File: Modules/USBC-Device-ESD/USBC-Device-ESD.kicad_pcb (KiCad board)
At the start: 4 copper layers, 4 parts, among them J1 USB-C, U2 USBLC6-2SC6

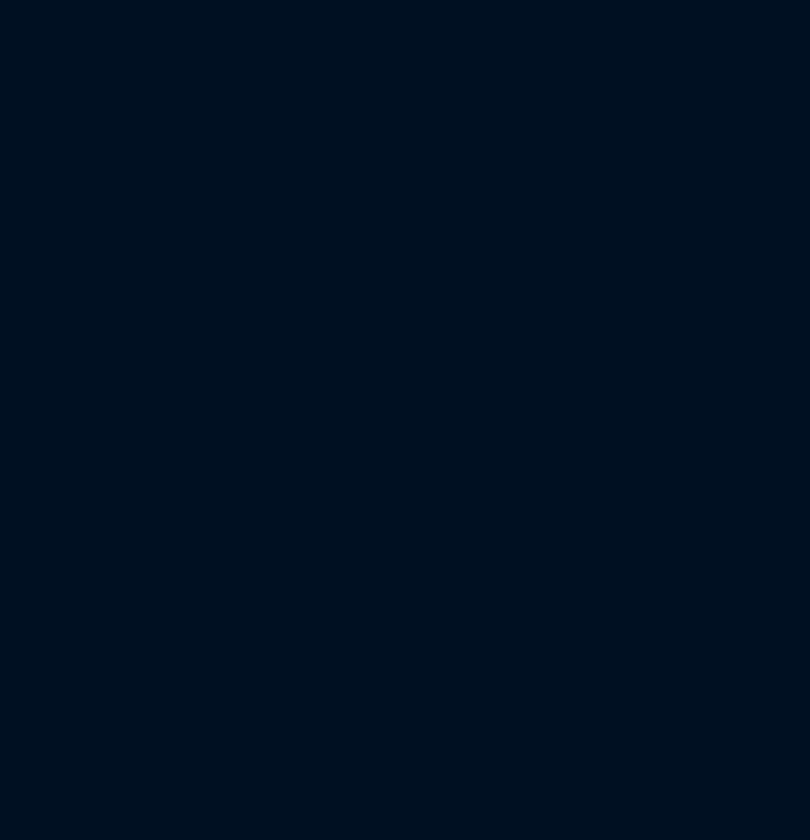
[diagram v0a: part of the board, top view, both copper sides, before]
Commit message: Add the base zones to five module boards
Whole-board zones for USBC, Buck, PowerMux, MCU and RF, written by file
before each board is opened. RF In1 carries a notch under J3 pad 1. Power
polygons become wide tracks during layout, because add_copper_pour cannot
set a zone priority.

Co-Authored-By: Claude Opus 5.5 (1M context) <noreply@anthropic.com>
Claude-Session: https://claude.ai/code/session_01ErAAfkmF4h3T5yfrw21utF
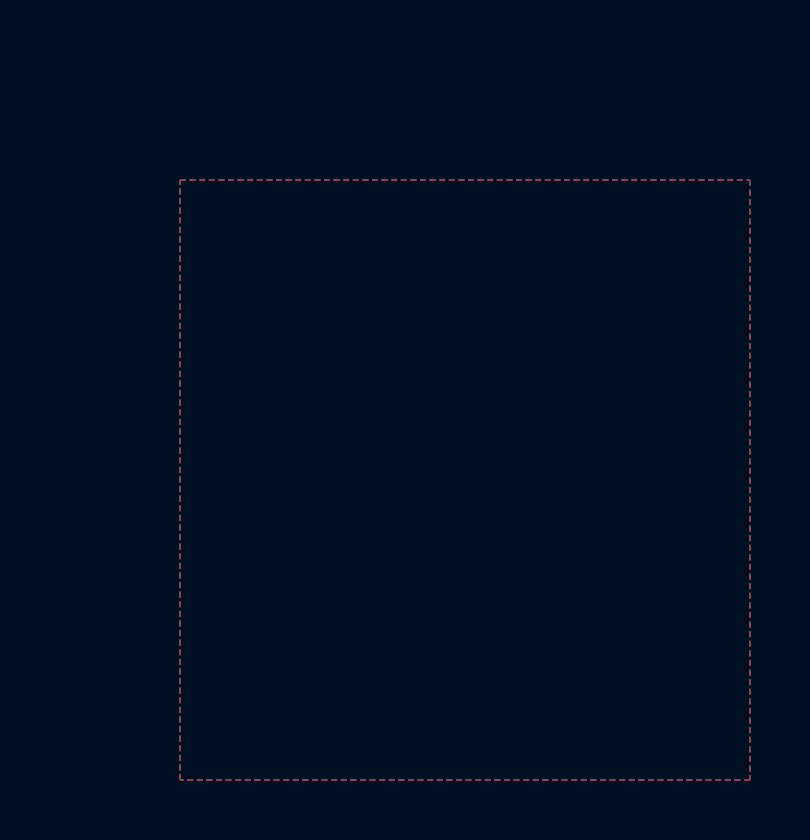
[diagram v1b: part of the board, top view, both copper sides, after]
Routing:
- added copper zone on B.Cu, net GND
- added copper zone on F.Cu, net GND
- added copper zone on In1.Cu, net GND
- added copper zone on In2.Cu, net GND
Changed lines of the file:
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@@
 	)
 	(embedded_fonts no)
-)
+  (zone (net 0) (net_name "GND") (layer "F.Cu")
+    (hatch edge 0.508)
+    (connect_pads (clearance 0.2))
+    (min_thickness 0.25)
+    (fill yes)
+    (polygon (pts
+      (xy 100.5 100.5)
+      (xy 119.5 100.5)
+      (xy 119.5 120.5)
+      (xy 100.5 120.5)
+    ))
+  )
+  (zone (net 0) (net_name "GND") (layer "In1.Cu")
+    (hatch edge 0.508)
+    (connect_pads (clearance 0.2))
+    (min_thickness 0.25)
+    (fill yes)
+    (polygon (pts
+      (xy 100.5 100.5)
+      (xy 119.5 100.5)
+      (xy 119.5 120.5)
+      (xy 100.5 120.5)
+    ))
+  )
+  (zone (net 0) (net_name "GND") (layer "In2.Cu")
+    (hatch edge 0.508)
+    (connect_pads (clearance 0.2))
+    (min_thickness 0.25)
+    (fill yes)
+    (polygon (pts
+      (xy 100.5 100.5)
+      (xy 119.5 100.5)
+      (xy 119.5 120.5)
+      (xy 100.5 120.5)
+    ))
+  )
+  (zone (net 0) (net_name "GND") (layer "B.Cu")
+    (hatch edge 0.508)
+    (connect_pads (clearance 0.2))
+    (min_thickness 0.25)
+    (fill yes)
+    (polygon (pts
+      (xy 100.5 100.5)
+      (xy 119.5 100.5)
+      (xy 119.5 120.5)
+      (xy 100.5 120.5)
+    ))
+  ))

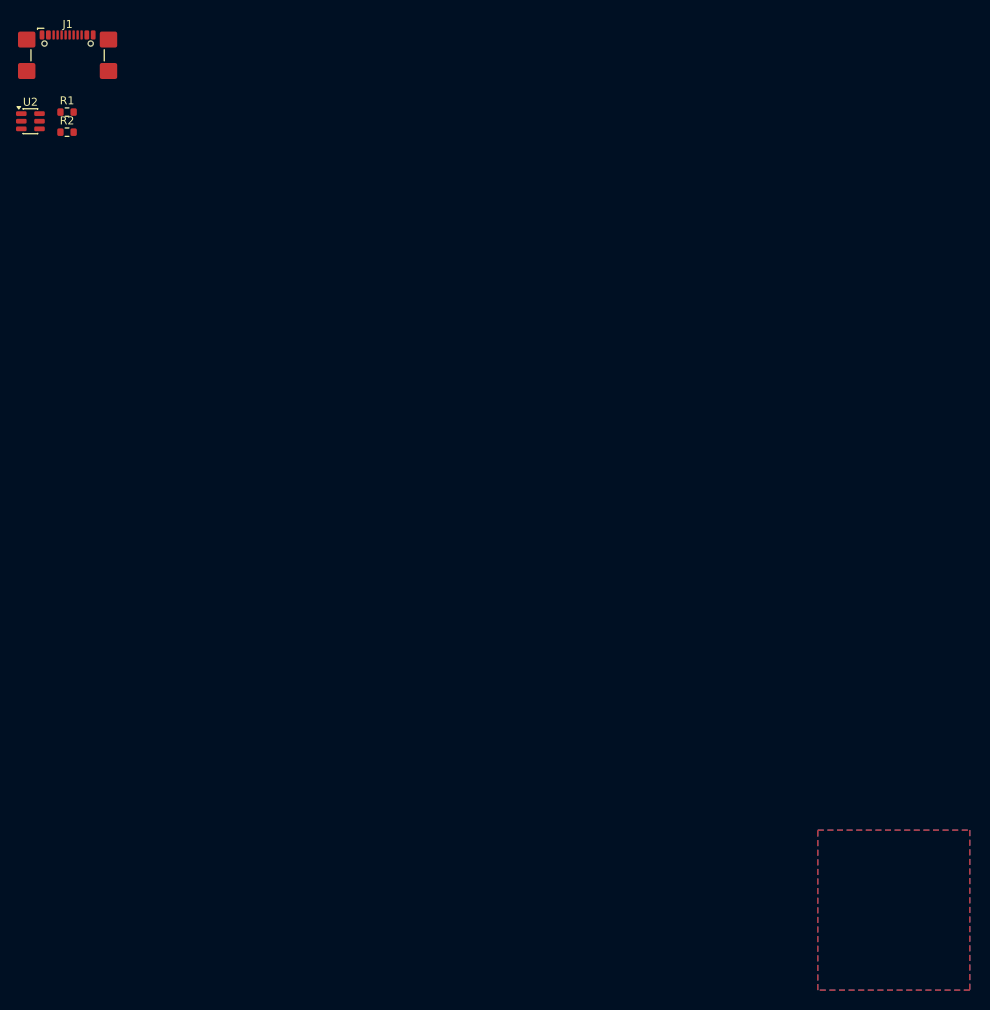
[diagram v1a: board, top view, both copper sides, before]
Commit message: Lay out the USBC-Device-ESD module
20 x 21 mm, 4 layers, GND on all four. J1 on the top edge, U2 in series in
the pair, the D+ crossing on a B.Cu jumper. VBUS at 0.508 mm with two vias
at each layer change. Breakout row at y 118.5: four GND, two VBUS, USB_DM,
USB_DP. Pair lengths 9.73 and 10.28 mm.

Rules: scope a 0.15 mm hole clearance to J1's own pads and pegs. The stock
GCT USB4110 land pattern sets them 0.194 mm apart.

DRC: 0 errors, 0 unconnected, 0 parity. The 4 track_dangling warnings are
the 4 interface stubs. Canary 8 to 252.

Co-Authored-By: Claude Opus 5.5 (1M context) <noreply@anthropic.com>
Claude-Session: https://claude.ai/code/session_01ErAAfkmF4h3T5yfrw21utF
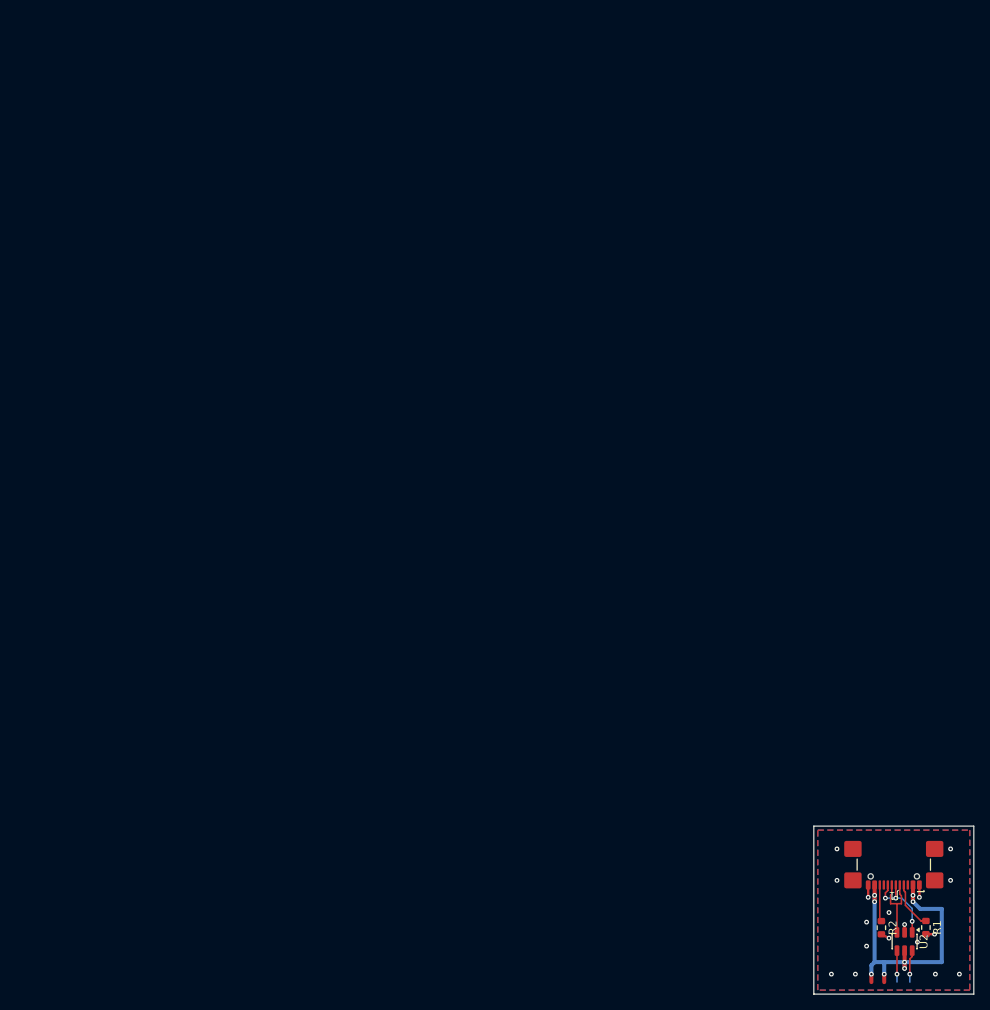
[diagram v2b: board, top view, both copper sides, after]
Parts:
- moved U2 149.8 mm to (111.3, 114.4), turned to -90 degrees
- moved R1 148.0 mm to (114.0, 112.7), turned to -90 degrees
- moved J1 143.0 mm to (110.0, 103.7), turned to 180 degrees
- moved R2 142.3 mm to (108.5, 112.7), turned to -90 degrees
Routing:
- net /VBUS: track 0.00 -> 40.6 mm, vias 0 -> 8
- net /USB_DP_CONN: track 0.00 -> 10.3 mm, vias 0 -> 3
- net /USB_DM_CONN: track 0.00 -> 9.77 mm
- net GND: track 0.00 -> 6.23 mm, vias 0 -> 17
- net /USB_CC1: track 0.00 -> 6.00 mm
- net /USB_CC2: track 0.00 -> 4.60 mm
- net /USB_DP: track 0.00 -> 4.06 mm, vias 0 -> 1
- net /USB_DM: track 0.00 -> 3.94 mm, vias 0 -> 1
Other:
- board outline added: 20 x 21 mm
- board text added: "GND"
- board text added: "USB_DM"
- board text added: "USB_DP"
- board text added: "VBUS"

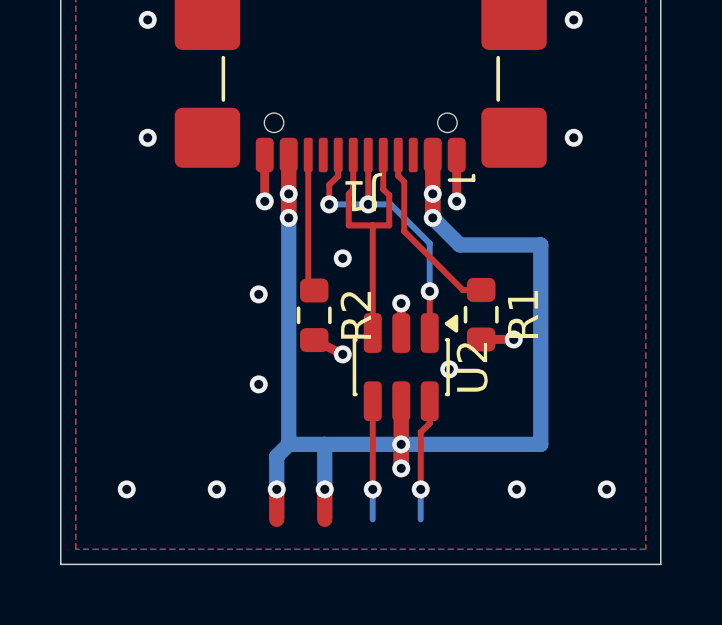
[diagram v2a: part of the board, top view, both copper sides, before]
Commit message: Restore footprints and move passive references to F.Fab
GUI batch 2a on all eight module boards. Update Footprints from Library
restores the (units) blocks that Konnect IPC writes dropped: U10, U1, SW1,
SW2 and U4 no longer report lib_footprint_mismatch. Reference designators of
C, R, L, FB, D, Y and TP parts move to F.Fab. U, J and SW stay on the silk.

Every board: DRC 0 errors, 0 unconnected, 0 parity, the canary fires, and
track_dangling equals the interface stub count.

Co-Authored-By: Claude Opus 5.5 (1M context) <noreply@anthropic.com>
Claude-Session: https://claude.ai/code/session_01ErAAfkmF4h3T5yfrw21utF
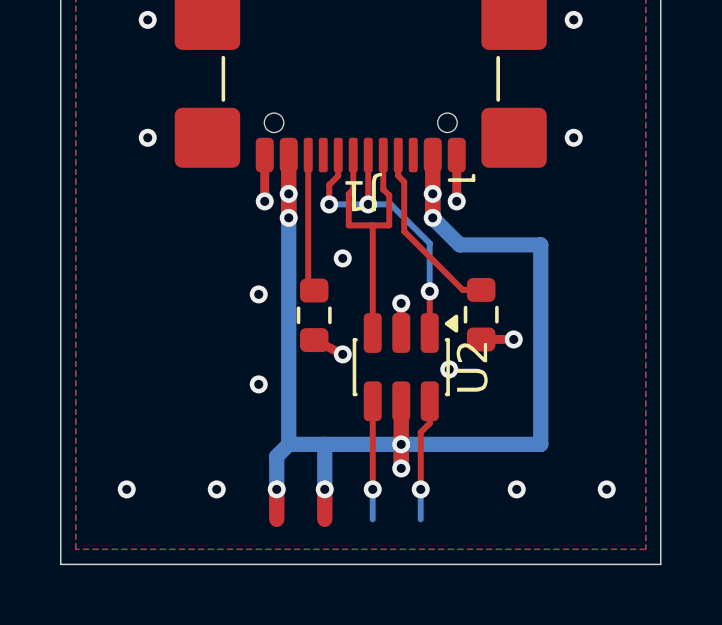
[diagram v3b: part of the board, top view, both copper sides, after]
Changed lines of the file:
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@@
 			(stroke
 				(width 0.12)
-				(type solid)
+				(type default)
 			)
 			(layer "F.SilkS")
@@
 			(stroke
 				(width 0.12)
-				(type solid)
+				(type default)
 			)
 			(layer "F.SilkS")
@@
 			(stroke
 				(width 0.12)
-				(type solid)
+				(type default)
 			)
 			(layer "F.SilkS")
@@
 			(stroke
 				(width 0.12)
-				(type solid)
+				(type default)
 			)
 			(layer "F.SilkS")
@@
 			(stroke
 				(width 0.1)
-				(type solid)
+				(type default)
 			)
 			(layer "Dwgs.User")
@@
 			(stroke
 				(width 0.05)
-				(type solid)
+				(type default)
 			)
 			(layer "F.CrtYd")
@@
 			(stroke
 				(width 0.05)
-				(type solid)
+				(type default)
 			)
 			(layer "F.CrtYd")
@@
 			(stroke
 				(width 0.05)
-				(type solid)
+				(type default)
 			)
 			(layer "F.CrtYd")
@@
 			(stroke
 				(width 0.05)
-				(type solid)
+				(type default)
 			)
 			(layer "F.CrtYd")
@@
 			(stroke
 				(width 0.05)
-				(type solid)
+				(type default)
 			)
 			(layer "F.CrtYd")
@@
 			(stroke
 				(width 0.05)
-				(type solid)
+				(type default)
 			)
 			(layer "F.CrtYd")
@@
 			(stroke
 				(width 0.05)
-				(type solid)
+				(type default)
 			)
 			(layer "F.CrtYd")
@@
 			(stroke
 				(width 0.05)
-				(type solid)
+				(type default)
 			)
 			(layer "F.CrtYd")
@@
 			(stroke
 				(width 0.05)
-				(type solid)
+				(type default)
 			)
 			(layer "F.CrtYd")
@@
 			(stroke
 				(width 0.05)
-				(type solid)
+				(type default)
 			)
 			(layer "F.CrtYd")
@@
 			(stroke
 				(width 0.05)
-				(type solid)
+				(type default)
 			)
 			(layer "F.CrtYd")
@@
 			(stroke
 				(width 0.05)
-				(type solid)
+				(type default)
 			)
 			(layer "F.CrtYd")
@@
 			(stroke
 				(width 0.05)
-				(type solid)
+				(type default)
 			)
 			(layer "F.CrtYd")
@@
 			(stroke
 				(width 0.05)
-				(type solid)
+				(type default)
 			)
 			(layer "F.CrtYd")
@@
 			(stroke
 				(width 0.05)
-				(type solid)
+				(type default)
 			)
 			(layer "F.CrtYd")
@@
 			(stroke
 				(width 0.05)
-				(type solid)
+				(type default)
 			)
 			(layer "F.CrtYd")
@@
 			(stroke
 				(width 0.05)
-				(type solid)
+				(type default)
 			)
 			(layer "F.CrtYd")
@@
 			(stroke
 				(width 0.05)
-				(type solid)
+				(type default)
 			)
 			(layer "F.CrtYd")
@@
 			(stroke
 				(width 0.05)
-				(type solid)
+				(type default)
 			)
 			(layer "F.CrtYd")
@@
 			(stroke
 				(width 0.05)
-				(type solid)
+				(type default)
 			)
 			(layer "F.CrtYd")
@@
 			(stroke
 				(width 0.1)
-				(type solid)
+				(type default)
 			)
 			(layer "F.Fab")
@@
 			(stroke
 				(width 0.1)
-				(type solid)
+				(type default)
 			)
 			(layer "F.Fab")
@@
 			(stroke
 				(width 0.1)
-				(type solid)
+				(type default)
 			)
 			(fill no)
@@
 		(tags "resistor")
 		(property "Reference" "R1"
-			(at 0 -1.43 -90)
-			(layer "F.SilkS")
+			(at 0 -1.43 270)
+			(layer "F.Fab")
 			(effects
 				(font
@@
 		)
 		(property "Value" "5.1k"
-			(at 0 1.43 -90)
+			(at 0 1.43 270)
 			(layer "F.Fab")
 			(effects
@@
 		)
 		(property "Datasheet" ""
-			(at 0 0 -90)
+			(at 0 0 270)
 			(layer "F.Fab")
 			(hide yes)
@@
 		)
 		(property "Description" ""
-			(at 0 0 -90)
+			(at 0 0 270)
 			(layer "F.Fab")
 			(hide yes)
@@
 		)
 		(property "KiLib_Generator" "SMD_2terminal_chip_molded"
-			(at 0 0 -90)
+			(at 0 0 270)
 			(layer "F.SilkS")
 			(hide yes)
@@
 		)
 		(property "MPN" "RC0603FR-075K1L"
-			(at 0 0 -90)
+			(at 0 0 270)
 			(unlocked yes)
 			(layer "F.Fab")
@@
 		)
 		(property "Manufacturer" "Yageo"
-			(at 0 0 -90)
+			(at 0 0 270)
 			(unlocked yes)
 			(layer "F.Fab")
@@
 		)
 		(fp_text user "${REFERENCE}"
-			(at 0 0 -90)
+			(at 0 0 270)
 			(layer "F.Fab")
 			(effects
@@
 		(tags "SOT TO_SOT_SMD")
 		(property "Reference" "U2"
-			(at 0 -2.4 -90)
+			(at 0 -2.4 270)
 			(layer "F.SilkS")
 			(effects
@@
 		)
 		(property "Value" "USBLC6-2SC6"
-			(at 0 2.4 -90)
+			(at 0 2.4 270)
 			(layer "F.Fab")
 			(effects
@@
 		)
 		(property "Datasheet" "https://www.st.com/resource/en/datasheet/usblc6-2.pdf"
-			(at 0 0 -90)
+			(at 0 0 270)
 			(layer "F.Fab")
 			(hide yes)
@@
 		)
 		(property "Description" ""
-			(at 0 0 -90)
+			(at 0 0 270)
 			(layer "F.Fab")
 			(hide yes)
@@
 		)
 		(property "KiLib_Generator" "package/gullwing"
-			(at 0 0 -90)
+			(at 0 0 270)
 			(layer "F.SilkS")
 			(hide yes)
@@
 		)
 		(property "MPN" "USBLC6-2SC6"
-			(at 0 0 -90)
+			(at 0 0 270)
 			(unlocked yes)
 			(layer "F.Fab")
@@
 		)
 		(property "Manufacturer" "STMicroelectronics"
-			(at 0 0 -90)
+			(at 0 0 270)
 			(unlocked yes)
 			(layer "F.Fab")
@@
 		(tags "resistor")
 		(property "Reference" "R2"
-			(at 0 -1.43 -90)
-			(layer "F.SilkS")
+			(at 0 -1.43 270)
+			(layer "F.Fab")
 			(effects
 				(font
@@
 		)
 		(property "Value" "5.1k"
-			(at 0 1.43 -90)
+			(at 0 1.43 270)
 			(layer "F.Fab")
 			(effects
@@
 		)
 		(property "Datasheet" ""
-			(at 0 0 -90)
+			(at 0 0 270)
 			(layer "F.Fab")
 			(hide yes)
@@
 		)
 		(property "Description" ""
-			(at 0 0 -90)
+			(at 0 0 270)
 			(layer "F.Fab")
 			(hide yes)
@@
 		)
 		(property "KiLib_Generator" "SMD_2terminal_chip_molded"
-			(at 0 0 -90)
+			(at 0 0 270)
 			(layer "F.SilkS")
 			(hide yes)
@@
 		)
 		(property "MPN" "RC0603FR-075K1L"
-			(at 0 0 -90)
+			(at 0 0 270)
 			(unlocked yes)
 			(layer "F.Fab")
@@
 		)
 		(property "Manufacturer" "Yageo"
-			(at 0 0 -90)
+			(at 0 0 270)
 			(unlocked yes)
 			(layer "F.Fab")
@@
 		)
 		(fp_text user "${REFERENCE}"
-			(at 0 0 -90)
-			(layer "F.Fab")
-			(effects
+			(at 0 0 270)
+			(layer "F.Fab")
+			(effects

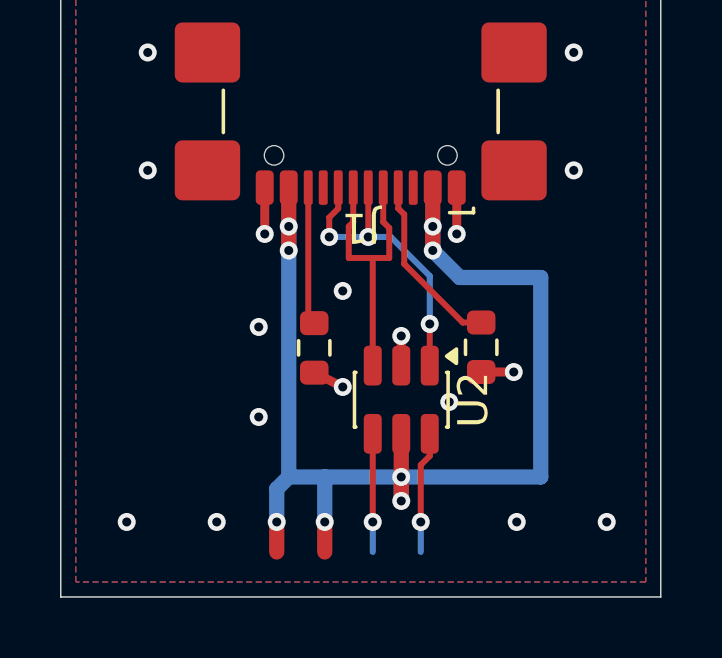
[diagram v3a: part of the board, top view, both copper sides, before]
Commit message: Apply the review fixes to five boards and set solid power pads
Plans were proven on scratch copies, then applied with KiCad's own pcbnew
Python API, so KiCad writes every file. Each board: DRC 0 errors, 0
unconnected, 0 parity, and the canary fires.

Ethernet and PoE module (R1-1, R1-2, R1-3):
- The fanout rule no longer matches zones.
- Chip-side copper keeps 1.0 mm from the line-side jack pads (was 0.26 mm):
  MDI_RDP, MDI_RDN, RCT and LED_LINK_K rerouted. A 1.0 mm rule enforces it.
  The VC1P lane passes J2.8 at 0.42 mm inside the jack pad field, and only
  that pair is excepted.
- GND vias: Ethernet 8 to 42, PoE 11 to 55. No starved thermal remains.

Buck (R2-2, R2-5): three GND vias at U8.1, C100.2 and C101.2. TP3 sits
against R61.1, with a courtyard rule scoped to that pair.
USBC (R2-4): U2 moves 3 mm toward J1, with two GND vias at U2.2.
MCU (R1-9): C2 sits 1.71 mm from U1 pin 3 (was 23.5 mm), with a courtyard
rule scoped to C2 and U1.
Solid zone connections (R2-3) on U8, L30, C100 to C104, C108 to C111 and J1.

Co-Authored-By: Claude Opus 5.5 (1M context) <noreply@anthropic.com>
Claude-Session: https://claude.ai/code/session_01ErAAfkmF4h3T5yfrw21utF
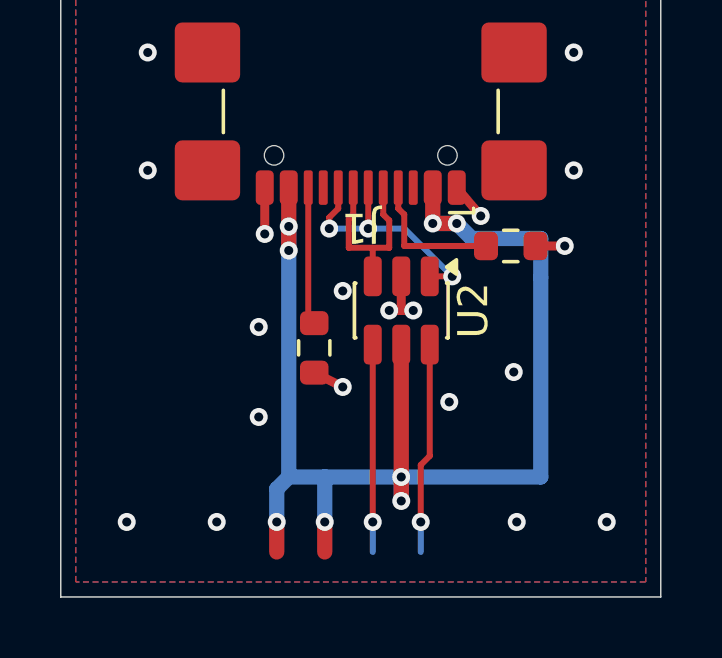
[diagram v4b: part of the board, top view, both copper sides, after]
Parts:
- moved R1 3.52 mm to (115.0, 109.3), turned to 0 degrees
- moved U2 2.97 mm to (111.3, 111.5)
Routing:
- net /USB_DM_CONN: track 9.77 -> 6.46 mm
- net /VBUS: track 40.6 -> 43.8 mm
- net /USB_DP: track 4.06 -> 7.04 mm
- net /USB_DM: track 3.94 -> 6.91 mm
- net /USB_DP_CONN: track 10.3 -> 8.36 mm
- net /USB_CC1: track 6.00 -> 4.75 mm
- net GND: track 6.23 -> 6.76 mm, vias 17 -> 19
